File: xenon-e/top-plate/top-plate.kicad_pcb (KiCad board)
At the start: 2 copper layers, 86.8 x 131.9 mm, 6 parts

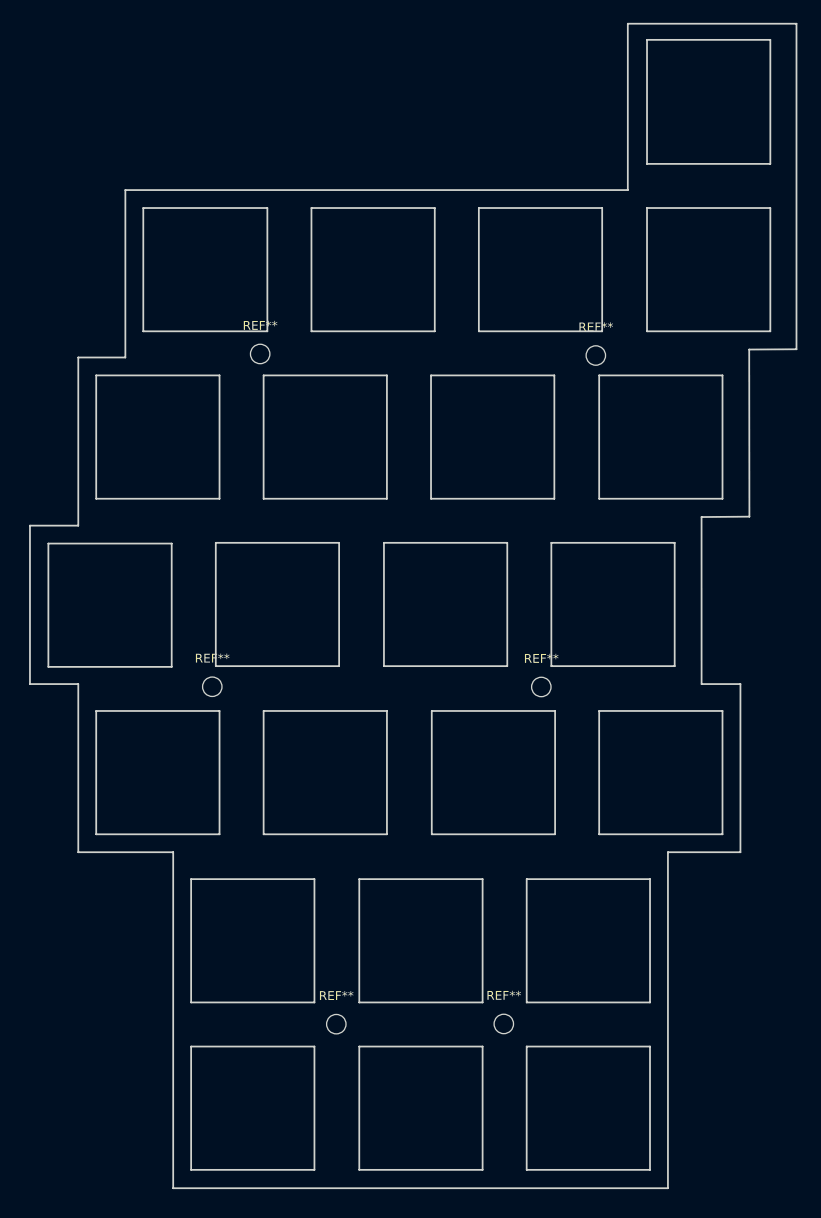
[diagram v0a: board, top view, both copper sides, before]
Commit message: Change mouting hole size
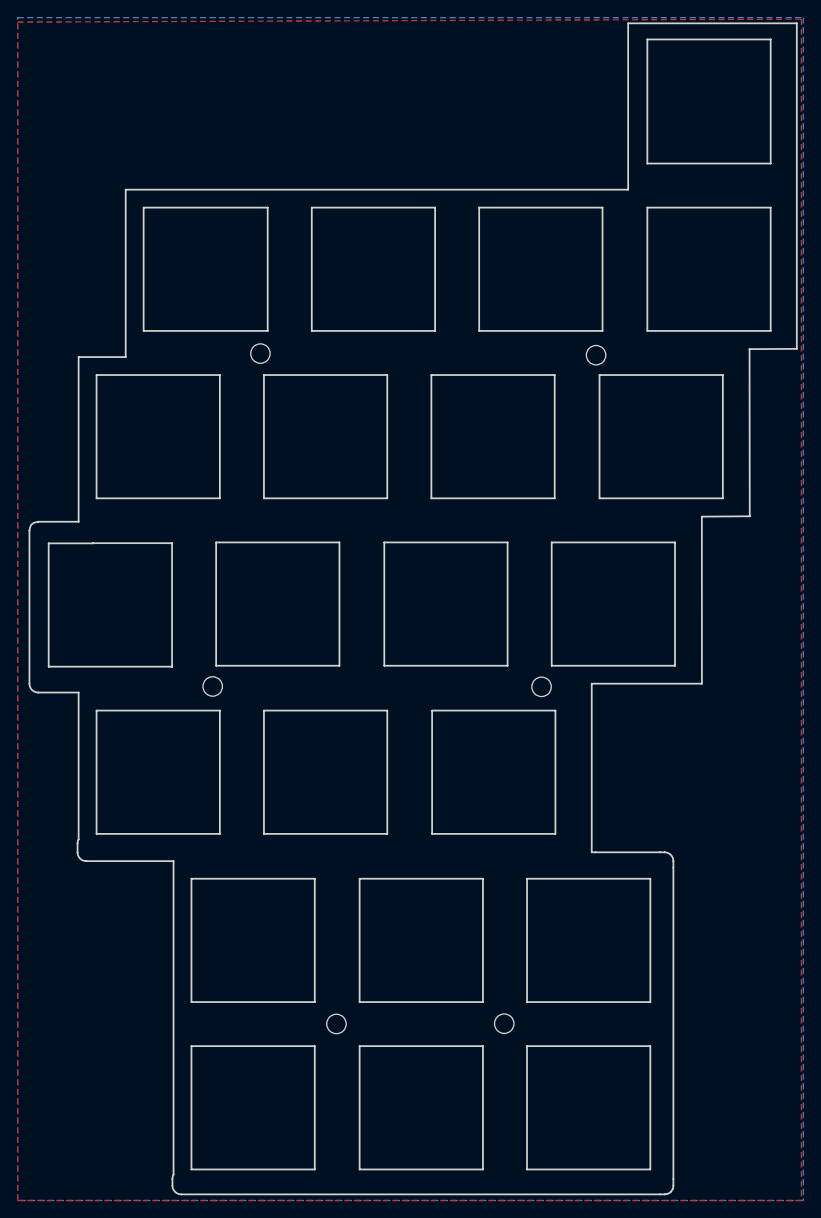
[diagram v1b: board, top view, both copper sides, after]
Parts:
- moved REF** 0.06 mm to (237.1, 138.0)
- moved REF** 0.06 mm to (204.1, 99.8)
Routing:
- added copper zone on B.Cu, net (none)
- added copper zone on F.Cu, net (none)
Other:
- board size 86.8 x 131.9 mm -> 86.9 x 132.7 mm
- board text added: "PCB designed by © narinari"
- board text added: "Xenon v1.2.0 + rotary"
